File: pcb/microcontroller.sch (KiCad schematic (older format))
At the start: 19 parts, among them U2 STM32F405RGTx, U3 TCAN330

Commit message: connectors, microcontroller
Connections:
- net UDB_DM renamed USB_DM
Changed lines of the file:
@@
 USB_DP
 Text HLabel 7650 3100 2    50   Input ~ 0
-UDB_DM
+USB_DM
 Wire Wire Line
 	6550 3000 7250 3000

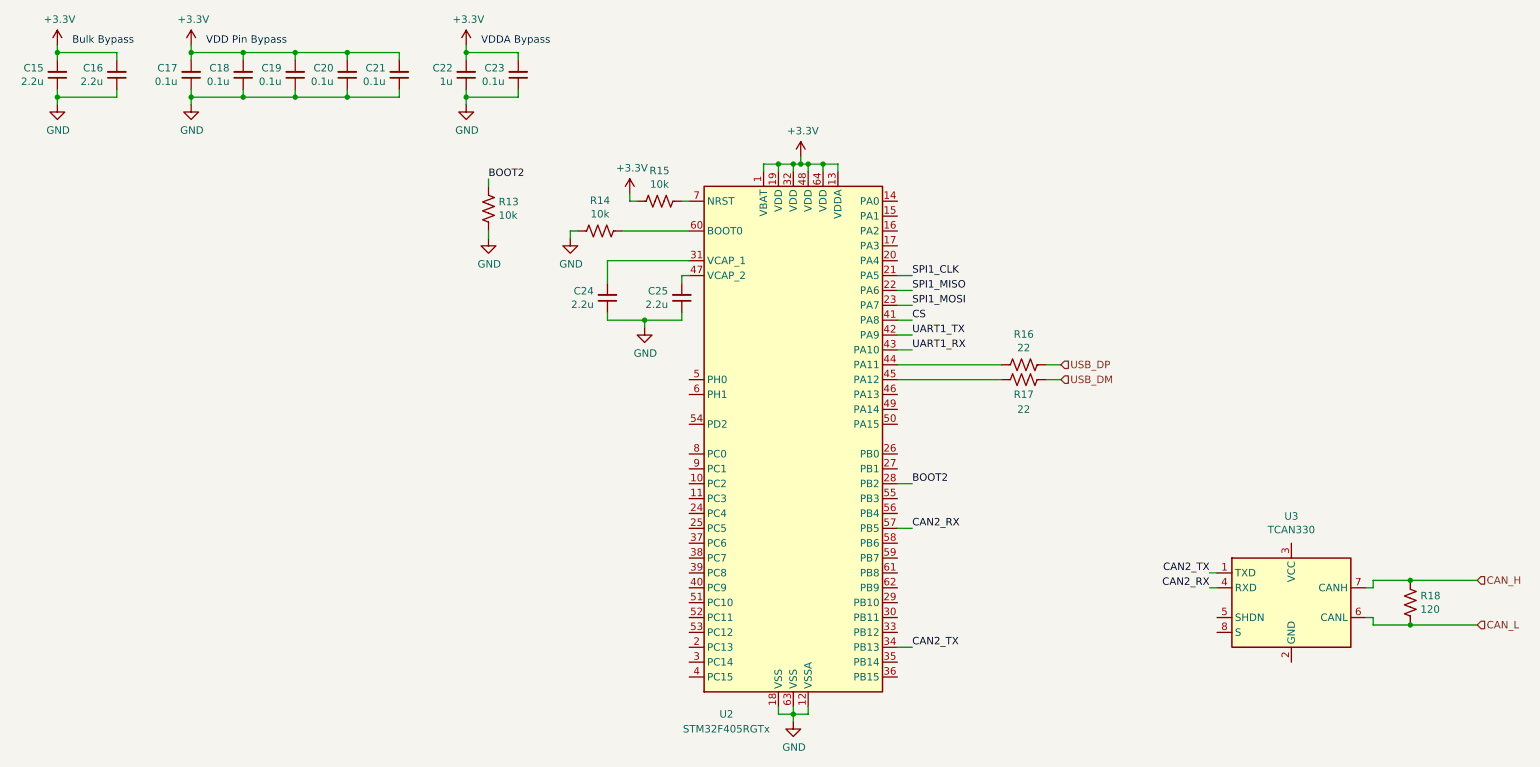
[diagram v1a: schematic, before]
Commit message: microcontroller added
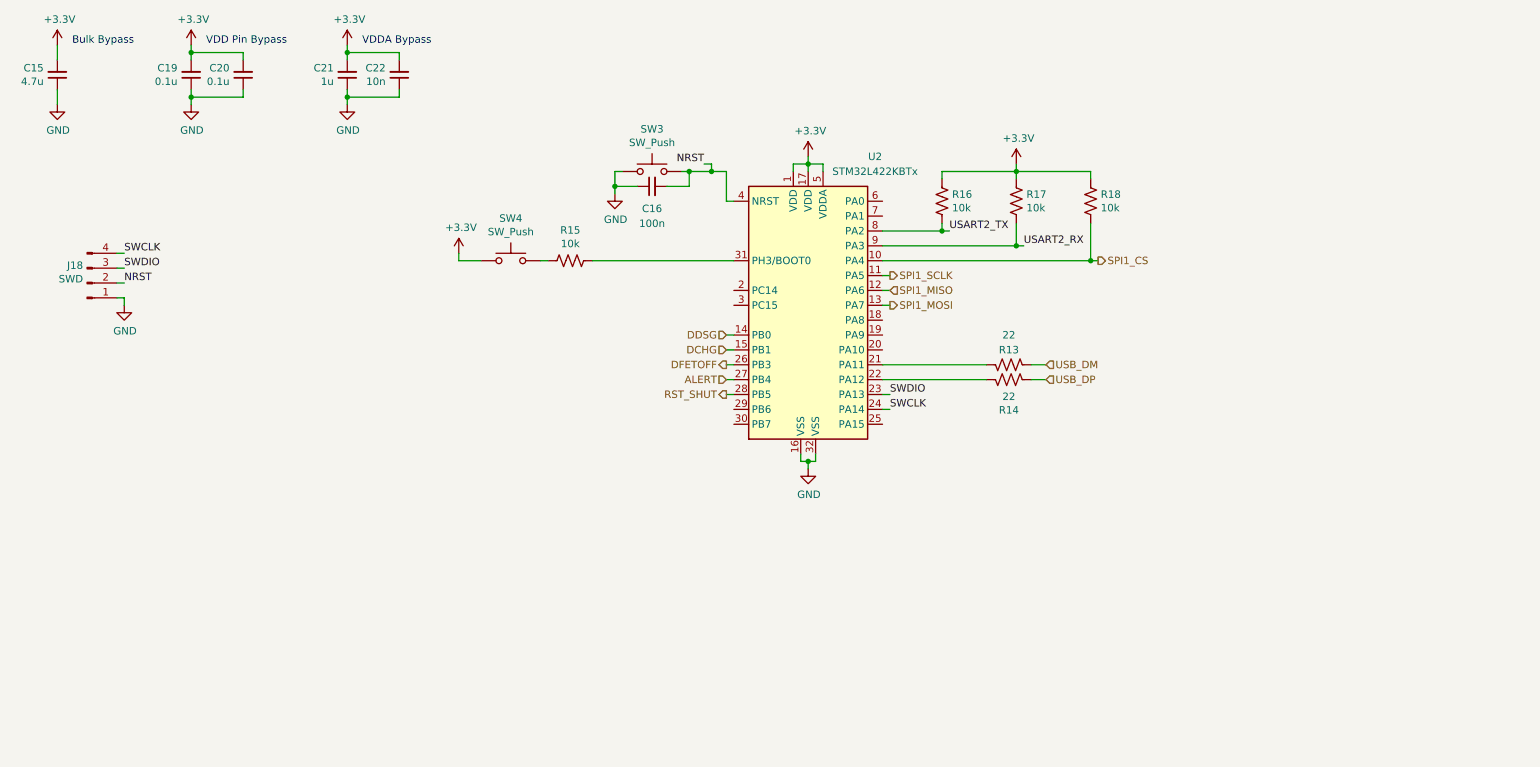
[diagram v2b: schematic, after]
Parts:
- removed C19, C20, C21: 0.1u, symbol Device:C_Small
- removed C24, C25: 2.2u, symbol Device:C_Small
- removed R13, R14: 10k, symbol Device:R_US
- removed U2: STM32F405RGTx, Package_QFP:LQFP-64_10x10mm_P0.5mm, symbol MCU_ST_STM32F4:STM32F405RGTx
- removed U3: TCAN330, symbol Interface_CAN_LIN:TCAN330
- added J18: SWD, symbol Connector:Conn_01x04_Male
- added R16, R17: 10k, Resistor_SMD:R_0805_2012Metric, symbol Device:R_US
- added SW3, SW4: SW_Push, symbol Switch:SW_Push
- added U2: STM32L422KBTx, Package_QFP:LQFP-32_7x7mm_P0.8mm, symbol MCU_ST_STM32L4:STM32L422KBTx
- C15: value 2.2u -> 4.7u; footprint (none) -> Capacitor_SMD:C_0805_2012Metric
- C16: value 2.2u -> 100n; footprint (none) -> Capacitor_SMD:C_0805_2012Metric
- C19: renamed from C17; footprint (none) -> Capacitor_SMD:C_0805_2012Metric
- C20: renamed from C18; footprint (none) -> Capacitor_SMD:C_0805_2012Metric
- C21: renamed from C22; footprint (none) -> Capacitor_SMD:C_0805_2012Metric
- C22: renamed from C23; value 0.1u -> 10n; footprint (none) -> Capacitor_SMD:C_0805_2012Metric
- R13: renamed from R17; footprint (none) -> Resistor_SMD:R_0805_2012Metric
- R14: renamed from R16; footprint (none) -> Resistor_SMD:R_0805_2012Metric
- R15: footprint (none) -> Resistor_SMD:R_0805_2012Metric
- R18: value 120 -> 10k; footprint (none) -> Resistor_SMD:R_0805_2012Metric
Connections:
- net CAN_H is gone; now on net +3V3: R18.1
- net +3V3: now also R16.1, R17.1, SW4.1, U2.1 (VDD), U2.17 (VDD), U2.5 (VDDA); no longer C16.2, R15.2
- net GND: now also J18.1 (Pin_1), SW3.1, U2.16 (VSS), U2.32 (VSS)
- net SPI1_MISO: now also U2.12 (PA6)
- net SPI1_MOSI: now also U2.13 (PA7)
- net at R15.1: now also U2.31 (PH3/BOOT0)
- net at R14.2: now also U2.22 (PA12)
- net at R13.2: now also U2.21 (PA11)
- net CAN_L renamed SPI1_CS
- net SPI1_CS: now also U2.10 (PA4)
- new net: R15.2, SW4.2
- new net ALERT: U2.27 (PB4)
- new net DCHG: U2.15 (PB1)
- new net DDSG: U2.14 (PB0)
- new net DFETOFF: U2.26 (PB3)
- new net NRST: C16.2, J18.2 (Pin_2), SW3.2, U2.4 (NRST)
- new net RST_SHUT: U2.28 (PB5)
- new net SPI1_SCLK: U2.11 (PA5)
- new net SWCLK: J18.4 (Pin_4), U2.24 (PA14)
- new net SWDIO: J18.3 (Pin_3), U2.23 (PA13)
- new net USART2_RX: R17.2, U2.9 (PA3)
- new net USART2_TX: R16.2, U2.8 (PA2)
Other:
- moved on the sheet: C21, C22, R13, R14
